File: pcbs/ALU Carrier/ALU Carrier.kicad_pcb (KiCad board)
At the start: 2 copper layers, 65 parts, among them J1001 Conn_02x20_Odd_Even, J1002 Conn_02x20_Odd_Even, U2001 74HC138, U6001 74HC14, U7001 74HC14, U7002 74HC08, U8001 74HC245, U8002 74HC245

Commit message: More experimental routing
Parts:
- moved U7001 206.9 mm to (77.5, 254.0)
- moved U7002 206.9 mm to (87.7, 254.6)
- moved D2001 39.6 mm to (114.3, 52.7)
- moved D2002 39.6 mm to (114.3, 55.2)
- moved D2003 39.6 mm to (114.3, 57.8)
- moved D2004 39.6 mm to (114.3, 60.3)
- moved D2005 39.6 mm to (114.3, 62.9)
- moved D2006 39.6 mm to (114.3, 65.4)
- moved D2007 39.6 mm to (114.3, 67.9)
- moved D2008 39.6 mm to (114.3, 70.5)
- moved R2001 39.6 mm to (110.5, 52.7)
- moved R2002 39.6 mm to (110.5, 55.2)
- moved R2003 39.6 mm to (110.5, 57.8)
- moved R2004 39.6 mm to (110.5, 60.3)
- moved R2005 39.6 mm to (110.5, 62.9)
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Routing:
- net /C15: track 43.9 -> 219.7 mm
- net /Instruction Decoder/I1: track 0.00 -> 171.1 mm
- net /C0: track 10.2 -> 174.6 mm
- net /Adder Subtractor/~{ADD}: track 211.2 -> 366.0 mm, vias 2 -> 3
- net /Instruction Decoder/I0: track 0.00 -> 146.9 mm
- net /Instruction Decoder/I3: track 0.00 -> 146.3 mm
- net /Instruction Decoder/I2: track 0.00 -> 146.3 mm
- net /C2: track 14.0 -> 152.7 mm
- net /C1: track 12.1 -> 116.2 mm
- net /Enabler/~{Enable}: track 127.9 -> 25.1 mm, vias 3 -> 2
- net /B8: track 244.0 -> 343.5 mm, vias 3 -> 4
- net /B14: track 261.1 -> 360.6 mm, vias 3 -> 4
- net /B10: track 249.7 -> 349.2 mm, vias 3 -> 4
- net /B12: track 255.4 -> 354.9 mm, vias 3 -> 4
- net /B9: track 242.1 -> 338.5 mm, vias 3 -> 4
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
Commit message: Thinking some more
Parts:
- added H1001: MountingHole, MountingHole:MountingHole_2.7mm_M2.5_ISO7380, F.Cu at (83.8, 33.0)
- added H1002: MountingHole, MountingHole:MountingHole_2.7mm_M2.5_ISO7380, F.Cu at (246.4, 33.0)
- added H1003: MountingHole, MountingHole:MountingHole_2.7mm_M2.5_ISO7380, F.Cu at (83.8, 259.1)
- added H1004: MountingHole, MountingHole:MountingHole_2.7mm_M2.5_ISO7380, F.Cu at (246.4, 259.1)
- moved U7002 174.0 mm to (102.9, 81.3)
- moved U7001 173.1 mm to (88.9, 81.3)
- moved R8001 85.1 mm to (243.8, 137.2)
- moved R8002 80.4 mm to (243.8, 139.7)
- moved R8003 75.7 mm to (243.8, 142.2)
- moved R8004 71.1 mm to (243.8, 144.8)
- moved R8007 69.5 mm to (243.8, 152.4)
- moved R8005 66.5 mm to (243.8, 147.3)
- moved R8008 64.8 mm to (243.8, 154.9)
- moved R8006 60.4 mm to (243.8, 149.9)
- moved R8012 60.4 mm to (243.8, 165.1)
- moved R8009 60.2 mm to (243.8, 157.5)
- moved D8002 55.9 mm to (240.0, 139.7)
- moved D8009 55.9 mm to (240.0, 157.5)
- moved D8013 55.9 mm to (240.0, 167.6)
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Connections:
- net /Enabler/Cycle0 renamed /Cycle0
- net /Enabler/Cycle1 renamed /Cycle1
- net /Enabler/Cycle2 renamed /Cycle2
- net /Enabler/Cycle3 renamed /Cycle3
- net /Enabler/Cycle4 renamed /Cycle4
- net /Instruction Decoder/I0 renamed /I0
- net /Instruction Decoder/I1 renamed /I1
- net /Instruction Decoder/I10 renamed /I10
- net /Instruction Decoder/I11 renamed /I11
- net /Instruction Decoder/I12 renamed /I12
- net /Instruction Decoder/I13 renamed /I13
- net /Instruction Decoder/I14 renamed /I14
- net /Instruction Decoder/I15 renamed /I15
- net /Instruction Decoder/I2 renamed /I2
- net /Instruction Decoder/I3 renamed /I3
- net /Instruction Decoder/I4 renamed /I4
- net /Instruction Decoder/I5 renamed /I5
- net /Instruction Decoder/I6 renamed /I6
- net /Instruction Decoder/I7 renamed /I7
- net /Instruction Decoder/I8 renamed /I8
- net /Instruction Decoder/I9 renamed /I9
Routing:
- net /Enabler/~{Enable}: track 25.1 -> 325.7 mm, vias 2 -> 7
- net /Cycle2: track 0.00 -> 184.6 mm, vias 0 -> 1
- net /Cycle3: track 0.00 -> 182.6 mm, vias 0 -> 1
- net /Comparator/~{Compare}: track 119.5 -> 232.5 mm, vias 2 -> 4
- net /Adder Subtractor/~{SUB}: track 183.2 -> 274.0 mm, vias 3 -> 5
- net /Adder Subtractor/~{ADD}: track 366.0 -> 313.3 mm, vias 3 -> 5
- net /B12: track 354.9 -> 303.9 mm
- net /A2: track 474.8 -> 429.1 mm
- net /C1: track 116.2 -> 71.7 mm
- net /B14: track 360.6 -> 316.6 mm
- net /I2: track 146.3 -> 181.9 mm, vias 0 -> 1
- net /C15: track 219.7 -> 184.1 mm
- net /I0: track 146.9 -> 181.9 mm, vias 0 -> 1
- net /I3: track 146.3 -> 179.9 mm, vias 0 -> 1
- net Net-(U2001-~{Y2}): track 41.1 -> 10.6 mm
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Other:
- board outline added: 177.8 x 241.3 mm

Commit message: Spotted nasty error in enable logic
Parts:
- moved D8017 221.6 mm to (205.7, 238.8), turned to 180 degrees
- moved R8017 217.9 mm to (201.9, 238.8), turned to 180 degrees
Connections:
- U2001 pad 4: /I3 -> GND
- U2001 pad 6: unconnected-(U2001-E2-Pad6) -> +5V
- U7001 pad 1: GND -> Net-(U7001-Pad1)
- U7001 pad 2: unconnected-(U7001-Pad2) -> /Enabler/~{Enable}
- U7001 pad 5: GND -> /I3
- U7001 pad 6: unconnected-(U7001-Pad6) -> Net-(U7001-Pad6)
- U7001 pad 8: unconnected-(U7001-Pad8) -> Net-(U7001-Pad8)
- U7001 pad 9: GND -> Net-(U7001-Pad9)
- U7002 pad 3: /Enabler/~{Enable} -> Net-(U7001-Pad9)
- U7002 pad 4: GND -> Net-(U7001-Pad8)
- U7002 pad 5: GND -> Net-(U7001-Pad6)
- U7002 pad 6: unconnected-(U7002-Pad6) -> Net-(U7001-Pad1)
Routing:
- net /C10: track 77.4 -> 191.0 mm
- net /C8: track 74.9 -> 188.4 mm
- net /C4: track 64.7 -> 178.3 mm
- net /C12: track 80.0 -> 193.5 mm
- net /C6: track 67.3 -> 180.8 mm
- net /C14: track 82.5 -> 196.1 mm
- net /C5: track 66.0 -> 176.5 mm
- net /C7: track 68.5 -> 179.0 mm
- net /C13: track 81.2 -> 191.7 mm
- net /C11: track 78.7 -> 189.2 mm
- net /C9: track 76.1 -> 186.6 mm
- net /C3: track 63.4 -> 173.9 mm
- net /C1: track 71.7 -> 171.4 mm
- net /Instruction Decoder/~{XOR}: track 169.9 -> 200.4 mm, vias 1 -> 3
- net /Instruction Decoder/~{NAND}: track 164.2 -> 193.4 mm, vias 2 -> 4
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- added copper zone on B.Cu, net +5V
- added copper zone on F.Cu, net GND
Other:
- board text added: "+5V"
- board text added: "ADD"
- board text added: "Arithmetic Logic Unit"
- board text added: "BSHFT"
- board text added: "C0"
- board text added: "C10"
- board text added: "C12"
- board text added: "C14"
- board text added: "C2"
- board text added: "C4"
- board text added: "C6"
- board text added: "C8"
- board text added: "CMP"
- board text added: "GND"
- board text added: "NAND"
- board text added: "RGE2025"
- board text added: "SUB"
- board text added: "XOR"

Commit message: Add part number placer
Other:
- board text added: "JLCJLCJLCJLC"
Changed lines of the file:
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@@
 		(tags "resistor")
 		(property "Reference" "R8017"
-			(at 0 -1.43 360)
+			(at 0 -1.43 0)
 			(layer "F.SilkS")
 			(hide yes)
@@
 		)
 		(property "Value" "4k7"
-			(at 0 1.43 360)
+			(at 0 1.43 0)
 			(layer "F.Fab")
 			(effects
@@
 		)
 		(fp_text user "${REFERENCE}"
-			(at 0 0 360)
+			(at 0 0 0)
 			(layer "F.Fab")
 			(effects
@@
 		(tags "LED")
 		(property "Reference" "D8017"
-			(at 0 -1.43 360)
+			(at 0 -1.43 0)
 			(layer "F.SilkS")
 			(hide yes)
@@
 		)
 		(property "Value" "Blue"
-			(at 0 1.43 360)
+			(at 0 1.43 0)
 			(layer "F.Fab")
 			(effects
@@
 		)
 		(fp_text user "${REFERENCE}"
-			(at 0 0 360)
+			(at 0 0 0)
 			(layer "F.Fab")
 			(effects
@@
 			)
 			(justify left mirror)
+		)
+	)
+	(gr_text "JLCJLCJLCJLC"
+		(at 242.57 259.08 0)
+		(layer "B.SilkS")
+		(effects
+			(font
+				(size 1.2192 1.2192)
+				(thickness 0.1524)
+			)
+			(justify left mirror)

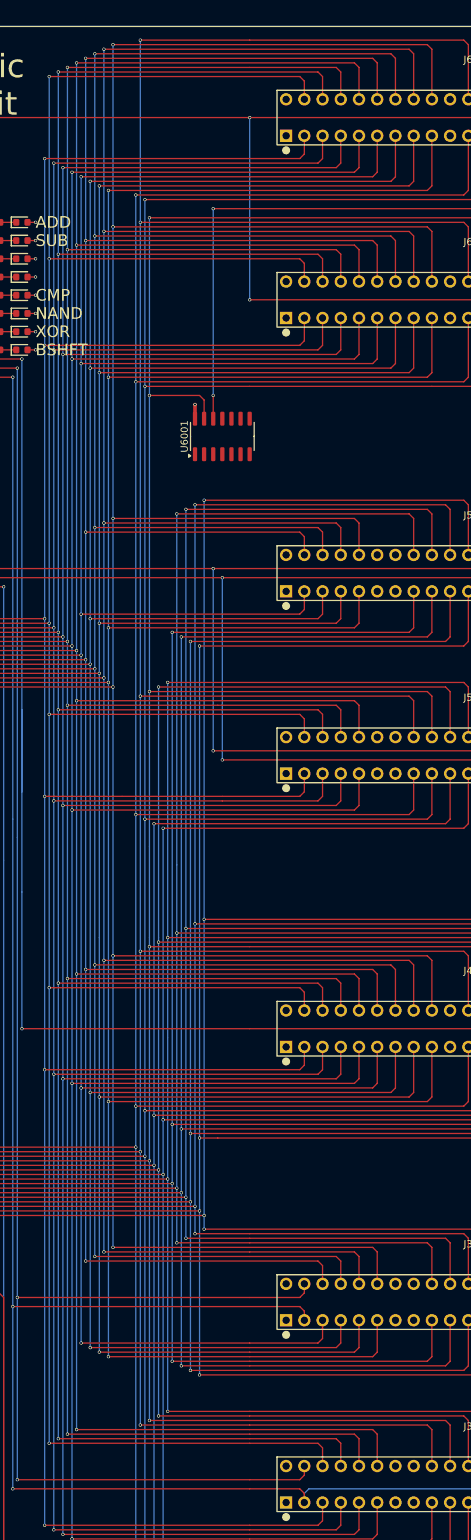
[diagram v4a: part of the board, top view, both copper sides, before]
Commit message: Fix for ALU Carrier (#16)
Fix the connections to the barrel shifter. A copy/paste error had left these the same for both of the connectors, when one was supposed to have the inputs rotated by 8 steps.

Also name the connectors on the silkscreen (closes #15 )
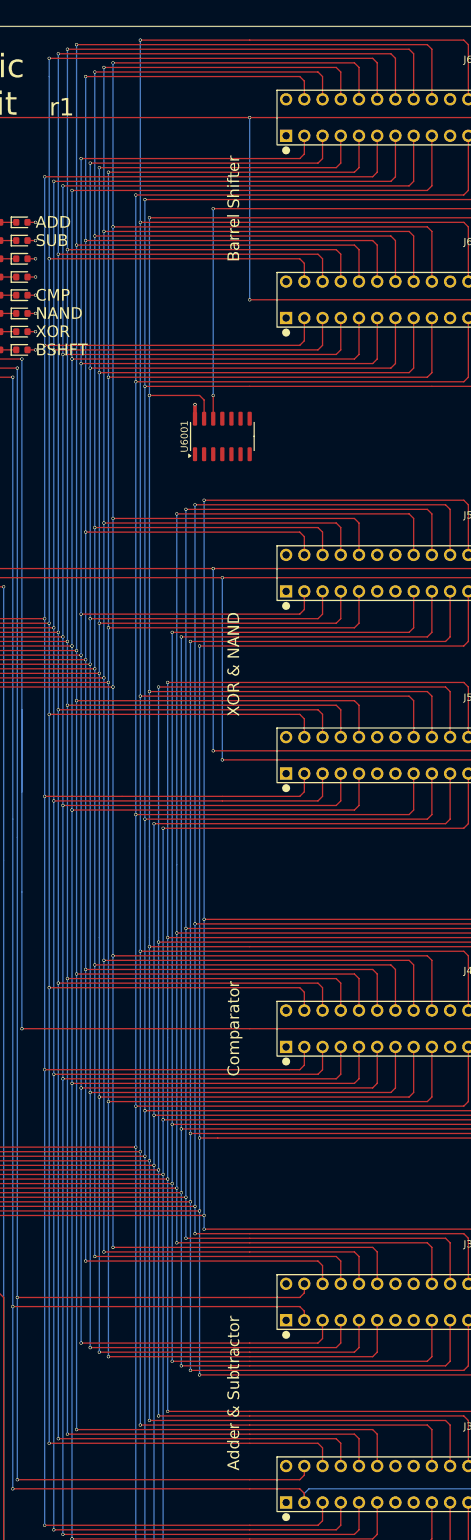
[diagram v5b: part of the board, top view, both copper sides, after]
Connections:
- J6002 pad A2: /A0 -> /A8
- J6002 pad A3: /A2 -> /A10
- J6002 pad A4: /A4 -> /A12
- J6002 pad A5: /A6 -> /A14
- J6002 pad A6: /A8 -> /A0
- J6002 pad A7: /A10 -> /A2
- J6002 pad A8: /A12 -> /A4
- J6002 pad A9: /A14 -> /A6
- J6002 pad B2: /A1 -> /A9
- J6002 pad B3: /A3 -> /A11
- J6002 pad B4: /A5 -> /A13
- J6002 pad B5: /A7 -> /A15
- J6002 pad B6: /A9 -> /A1
- J6002 pad B7: /A11 -> /A3
- J6002 pad B8: /A13 -> /A5
- J6002 pad B9: /A15 -> /A7
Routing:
- net /A5: track 455.9 -> 471.1 mm
- net /A3: track 443.8 -> 459.0 mm
- net /A11: track 443.8 -> 428.6 mm
- net /A7: track 467.9 -> 483.2 mm
- net /A15: track 467.9 -> 452.7 mm
- net /A13: track 455.9 -> 440.6 mm
- net /A1: track 431.7 -> 447.0 mm
- net /A9: track 431.7 -> 416.5 mm
- net /A10: track 444.3 -> 434.2 mm
- net /A2: track 449.4 -> 459.6 mm
- net /A0: track 437.3 -> 447.5 mm
- net /A8: track 432.3 -> 422.1 mm
- net /A6: track 473.5 -> 483.7 mm
- net /A4: track 461.5 -> 471.6 mm
- net /A14: track 468.5 -> 458.3 mm
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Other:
- board text added: "Adder & Subtractor"
- board text added: "Barrel Shifter"
- board text added: "Comparator"
- board text added: "XOR & NAND"
- board text added: "r${REVISION}"
